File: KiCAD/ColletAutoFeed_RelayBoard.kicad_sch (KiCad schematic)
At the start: 2 parts, among them J1 690367191672, U2 ProS3

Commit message: Added 24v Monitor Circuit
Added hierarchical sheet with 24v monitor circuit. Added 4 pin power connector for 24v input. Same family connector as ribbon cable connector for relay to solenoid connections out to daughter board.
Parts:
- added J2: 690367190472, 690367190472:690367190472, symbol WR-MM-4-Female:690367190472
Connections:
- net GND: now also J2.2, J2.4
- net IO12: now reaches U2.17 (IO12)
- new net +24V: J2.1, J2.3
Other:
- added sheet 24v Monitor Circuit (24v_Monitor_Circuit.kicad_sch)
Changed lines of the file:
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@@
   (junction (at 60.96 135.89) (diameter 0) (color 0 0 0 0)
   )
+  (junction (at 100.33 135.89) (diameter 0) (color 0 0 0 0)
+  )
   (junction (at 45.72 135.89) (diameter 0) (color 0 0 0 0)
   )
   (junction (at 40.64 135.89) (diameter 0) (color 0 0 0 0)
   )
+  (junction (at 102.87 125.73) (diameter 0) (color 0 0 0 0)
+  )
   (junction (at 71.12 135.89) (diameter 0) (color 0 0 0 0)
   )
@@
     (stroke (width 0) (type default))
   )
+  (wire (pts (xy 97.79 125.73) (xy 102.87 125.73))
+    (stroke (width 0) (type default))
+  )
   (wire (pts (xy 182.88 95.25) (xy 182.88 104.14))
     (stroke (width 0) (type default))
@@
     (stroke (width 0) (type default))
   )
+  (wire (pts (xy 95.25 135.89) (xy 100.33 135.89))
+    (stroke (width 0) (type default))
+  )
   (wire (pts (xy 135.89 71.12) (xy 135.89 81.28))
     (stroke (width 0) (type default))
@@
     (stroke (width 0) (type default))
   )
+  (wire (pts (xy 85.09 27.94) (xy 96.52 27.94))
+    (stroke (width 0) (type default))
+  )
   (wire (pts (xy 45.72 135.89) (xy 50.8 135.89))
     (stroke (width 0) (type default))
@@
     (stroke (width 0) (type default))
   )
+  (wire (pts (xy 85.09 35.56) (xy 96.52 35.56))
+    (stroke (width 0) (type default))
+  )
   (wire (pts (xy 55.88 135.89) (xy 60.96 135.89))
     (stroke (width 0) (type default))
   )
+  (wire (pts (xy 25.4 45.72) (xy 25.4 57.15))
+    (stroke (width 0) (type default))
+  )
   (wire (pts (xy 179.07 71.12) (xy 179.07 81.28))
     (stroke (width 0) (type default))
@@
     (effects (font (size 1.27 1.27)) (justify left bottom))
   )
+  (label "IO12" (at 85.09 35.56 0) (fields_autoplaced)
+    (effects (font (size 1.27 1.27)) (justify left bottom))
+  )
   (label "IO0" (at 153.67 71.12 270) (fields_autoplaced)
     (effects (font (size 1.27 1.27)) (justify right bottom))
@@
     (effects (font (size 1.27 1.27)) (justify right bottom))
   )
+  (label "IO12" (at 25.4 57.15 90) (fields_autoplaced)
+    (effects (font (size 1.27 1.27)) (justify left bottom))
+  )
   (label "S4" (at 96.52 104.14 90) (fields_autoplaced)
     (effects (font (size 1.27 1.27)) (justify left bottom))
@@
   )
   (label "IO4" (at 48.26 57.15 90) (fields_autoplaced)
+    (effects (font (size 1.27 1.27)) (justify left bottom))
+  )
+  (label "MCU 3.3v" (at 85.09 27.94 0) (fields_autoplaced)
     (effects (font (size 1.27 1.27)) (justify left bottom))
   )
@@
     )
   )
+  (symbol (lib_id "power:GND") (at 100.33 135.89 0) (unit 1)
+    (in_bom yes) (on_board yes) (dnp no) (fields_autoplaced)
+    (property "Reference" "#PWR013" (at 100.33 142.24 0)
+      (effects (font (size 1.27 1.27)) hide)
+    )
+    (property "Value" "GND" (at 100.33 140.97 0)
+      (effects (font (size 1.27 1.27)))
+    )
+    (property "Footprint" "" (at 100.33 135.89 0)
+      (effects (font (size 1.27 1.27)) hide)
+    )
+    (property "Datasheet" "" (at 100.33 135.89 0)
+      (effects (font (size 1.27 1.27)) hide)
+    )
+    (pin "1")
+    (instances
+      (project "ColletAutoFeed_RelayBoard"
+        (path "/603d0a2e-fca7-40af-8fa8-51b59d823d4d"
+          (reference "#PWR013") (unit 1)
+        )
+      )
+    )
+  )
+  (symbol (lib_id "WR-MM-4-Female:690367190472") (at 100.33 130.81 0) (unit 1)
+    (in_bom yes) (on_board yes) (dnp no) (fields_autoplaced)
+    (property "Reference" "J2" (at 105.41 129.54 0)
+      (effects (font (size 1.27 1.27)) (justify left))
+    )
+    (property "Value" "690367190472" (at 105.41 132.08 0)
+      (effects (font (size 1.27 1.27)) (justify left))
+    )
+    (property "Footprint" "690367190472:690367190472" (at 100.33 130.81 0)
+      (effects (font (size 1.27 1.27)) (justify bottom) hide)
+    )
+    (property "Datasheet" "" (at 100.33 130.81 0)
+      (effects (font (size 1.27 1.27)) hide)
+    )
+    (property "MF" "Wurth Elektronik" (at 100.33 130.81 0)
+      (effects (font (size 1.27 1.27)) (justify bottom) hide)
+    )
+    (property "Description" "\n4 Position Receptacle Connector 0.100 (2.54mm) Through Hole Tin\n" (at 100.33 130.81 0)
+      (effects (font (size 1.27 1.27)) (justify bottom) hide)
+    )
+    (property "Package" "None" (at 100.33 130.81 0)
+      (effects (font (size 1.27 1.27)) (justify bottom) hide)
+    )
+    (property "Purchase-URL" "https://www.snapeda.com/api/url_track_click_mouser/?unipart_id=4618894&manufacturer=Wurth Elektronik&part_name=690367190472&search_term=690367190472" (at 100.33 130.81 0)
+      (effects (font (size 1.27 1.27)) (justify bottom) hide)
+    )
+    (property "GENDER" "Female" (at 100.33 130.81 0)
+      (effects (font (size 1.27 1.27)) (justify bottom) hide)
+    )
+    (property "Price" "None" (at 100.33 130.81 0)
+      (effects (font (size 1.27 1.27)) (justify bottom) hide)
+    )
+    (property "IR" "1.5A" (at 100.33 130.81 0)
+      (effects (font (size 1.27 1.27)) (justify bottom) hide)
+    )
+    (property "VALUE" "690367190472" (at 100.33 130.81 0)
+      (effects (font (size 1.27 1.27)) (justify bottom) hide)
+    )
+    (property "PACKAGING" "Tube" (at 100.33 130.81 0)
+      (effects (font (size 1.27 1.27)) (justify bottom) hide)
+    )
+    (property "PINS" "4" (at 100.33 130.81 0)
+      (effects (font (size 1.27 1.27)) (justify bottom) hide)
+    )
+    (property "SnapEDA_Link" "https://www.snapeda.com/parts/690367190472/Wurth+Elektronik/view-part/?ref=snap" (at 100.33 130.81 0)
+      (effects (font (size 1.27 1.27)) (justify bottom) hide)
+    )
+    (property "DATASHEET-URL" "https://www.we-online.com/catalog/datasheet/690367190472.pdf" (at 100.33 130.81 0)
+      (effects (font (size 1.27 1.27)) (justify bottom) hide)
+    )
+    (property "MP" "690367190472" (at 100.33 130.81 0)
+      (effects (font (size 1.27 1.27)) (justify bottom) hide)
+    )
+    (property "PITCH" "2.54" (at 100.33 130.81 0)
+      (effects (font (size 1.27 1.27)) (justify bottom) hide)
+    )
+    (property "PART-NUMBER" "690367190472" (at 100.33 130.81 0)
+      (effects (font (size 1.27 1.27)) (justify bottom) hide)
+    )
+    (property "TYPE" "Straight" (at 100.33 130.81 0)
+      (effects (font (size 1.27 1.27)) (justify bottom) hide)
+    )
+    (property "Availability" "In Stock" (at 100.33 130.81 0)
+      (effects (font (size 1.27 1.27)) (justify bottom) hide)
+    )
+    (property "Check_prices" "https://www.snapeda.com/parts/690367190472/Wurth+Elektronik/view-part/?ref=eda" (at 100.33 130.81 0)
+      (effects (font (size 1.27 1.27)) (justify bottom) hide)
+    )
+    (pin "2")
+    (pin "3")
+    (pin "1")
+    (pin "4")
+    (instances
+      (project "ColletAutoFeed_RelayBoard"
+        (path "/603d0a2e-fca7-40af-8fa8-51b59d823d4d"
+          (reference "J2") (unit 1)
+        )
+      )
+    )
+  )
   (symbol (lib_id "power:GND") (at 71.12 135.89 0) (unit 1)
     (in_bom yes) (on_board yes) (dnp no) (fields_autoplaced)
@@
         (path "/603d0a2e-fca7-40af-8fa8-51b59d823d4d"
           (reference "#PWR01") (unit 1)
+        )
+      )
+    )
+  )
+  (symbol (lib_id "power:+24V") (at 102.87 125.73 0) (unit 1)
+    (in_bom yes) (on_board yes) (dnp no) (fields_autoplaced)
+    (property "Reference" "#PWR014" (at 102.87 129.54 0)
+      (effects (font (size 1.27 1.27)) hide)
+    )
+    (property "Value" "+24V" (at 102.87 120.65 0)
+      (effects (font (size 1.27 1.27)))
+    )
+    (property "Footprint" "" (at 102.87 125.73 0)
+      (effects (font (size 1.27 1.27)) hide)
+    )
+    (property "Datasheet" "" (at 102.87 125.73 0)
+      (effects (font (size 1.27 1.27)) hide)
+    )
+    (pin "1")
+    (instances
+      (project "ColletAutoFeed_RelayBoard"
+        (path "/603d0a2e-fca7-40af-8fa8-51b59d823d4d"
+          (reference "#PWR014") (unit 1)
         )
       )
@@
       )
     )
+  )
+  (sheet (at 96.52 25.4) (size 12.7 13.97) (fields_autoplaced)
+    (stroke (width 0.1524) (type solid))
+    (fill (color 0 0 0 0.0000))
+    (property "Sheetname" "24v Monitor Circuit" (at 96.52 24.6884 0)
+      (effects (font (size 1.27 1.27)) (justify left bottom))
+    )
+    (property "Sheetfile" "24v_Monitor_Circuit.kicad_sch" (at 96.52 39.9546 0)
+      (effects (font (size 1.27 1.27)) (justify left top))
+    )
+    (pin "MCU 3.3v" input (at 96.52 27.94 180)
+      (effects (font (size 1.27 1.27)) (justify left))
+    )
+    (pin "MCU GPIO" output (at 96.52 35.56 180)
+      (effects (font (size 1.27 1.27)) (justify left))
+    )
+    (instances
+      (project "ColletAutoFeed_RelayBoard"
+        (path "/603d0a2e-fca7-40af-8fa8-51b59d823d4d" (page "10"))
+      )
+    )

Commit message: Ran Annotation and ERC
Annotated and ran Electronics Rules Checker. Started assigning footprints and appropriate step files to said footprints. Added custom KiCAD library folder to Github.
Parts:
- removed J1: 690367191672, 690367191672:690367191672, symbol WR-MM-16-Female:690367191672
- removed J2: 690367190472, 690367190472:690367190472, symbol WR-MM-4-Female:690367190472
- removed U2: ProS3, symbol ProS3:ProS3
- added J1: 690367191672, WR-MM:690367191672, symbol WR-MM-16:690367191672
- added J2: 690367190472, WR-MM:690367190472, symbol WR-MM-04:690367190472
- added U1: ProS3, ProS3:ProS3_TH, symbol ProS3:ProS3
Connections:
- net +24V: now also J2.1, J2.3
- net GND: now also J1.10, J1.12, J1.14, J1.16, J1.2, J1.4, J1.6, J1.8, J2.2, J2.4
- net IO0: now also U1.11 (IO0)
- net IO1: now also U1.5 (IO1)
- net IO12: now also U1.17 (IO12)
- net IO16: now also U1.13 (IO16)
- net IO2: now also U1.6 (IO2)
- net IO21: now also U1.10 (IO21)
- net IO3: now also U1.7 (IO3)
- net IO4: now also U1.8 (IO4)
- net IO5: now also U1.9 (IO5)
- net MCU 3.3v: now also U1.4 (3V3)
- net S1: now also J1.1
- net S2: now also J1.3
- net S3: now also J1.5
- net S4: now also J1.7
- net S5: now also J1.9
- net S6: now also J1.11
- net S7: now also J1.13
- net S8: now also J1.15
- no-connect marks 0 -> 24

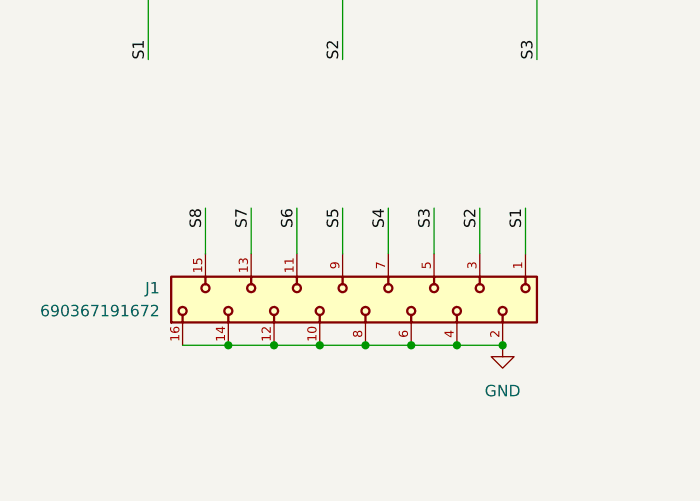
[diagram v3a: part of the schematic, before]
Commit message: Switched to TE AMP-Latch connector
Removed Wurth ribbon cable connector and replaced with TE AMP-Latch connector after physically evaluating both.
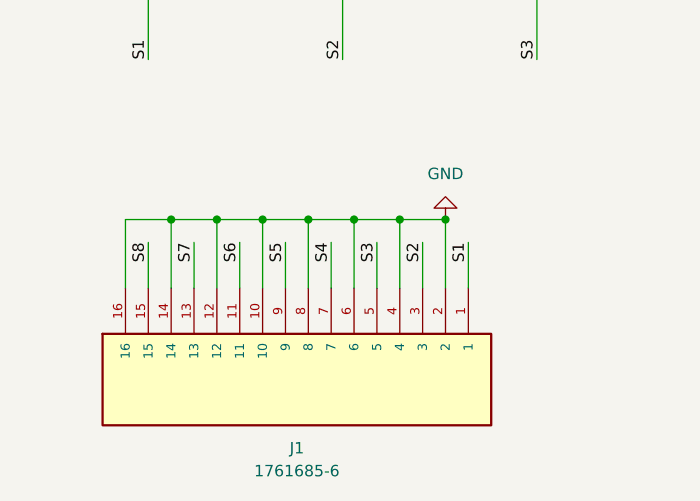
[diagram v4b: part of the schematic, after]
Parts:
- removed J1: 690367191672, WR-MM:690367191672, symbol WR-MM-16:690367191672
- added J1: 1761685-6, 1761685-6:TE_1761685-6, symbol Vertical Header - Locking:1761685-6
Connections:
- net GND: now also J1.10, J1.12, J1.14, J1.16, J1.2, J1.4, J1.6, J1.8
- net S1: now also J1.1
- net S2: now also J1.3
- net S3: now also J1.5
- net S4: now also J1.7
- net S5: now also J1.9
- net S6: now also J1.11
- net S7: now also J1.13
- net S8: now also J1.15

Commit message: Assigned footprint to pin header
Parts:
- J1: footprint 1761685-6:TE_1761685-6 -> Vertical Header - Locking:TE_1761685-6
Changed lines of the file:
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@@
       (effects (font (size 1.27 1.27)))
     )
-    (property "Footprint" "1761685-6:TE_1761685-6" (at 46.99 139.7 0)
+    (property "Footprint" "Vertical Header - Locking:TE_1761685-6" (at 46.99 139.7 0)
       (effects (font (size 1.27 1.27)) (justify bottom) hide)
     )

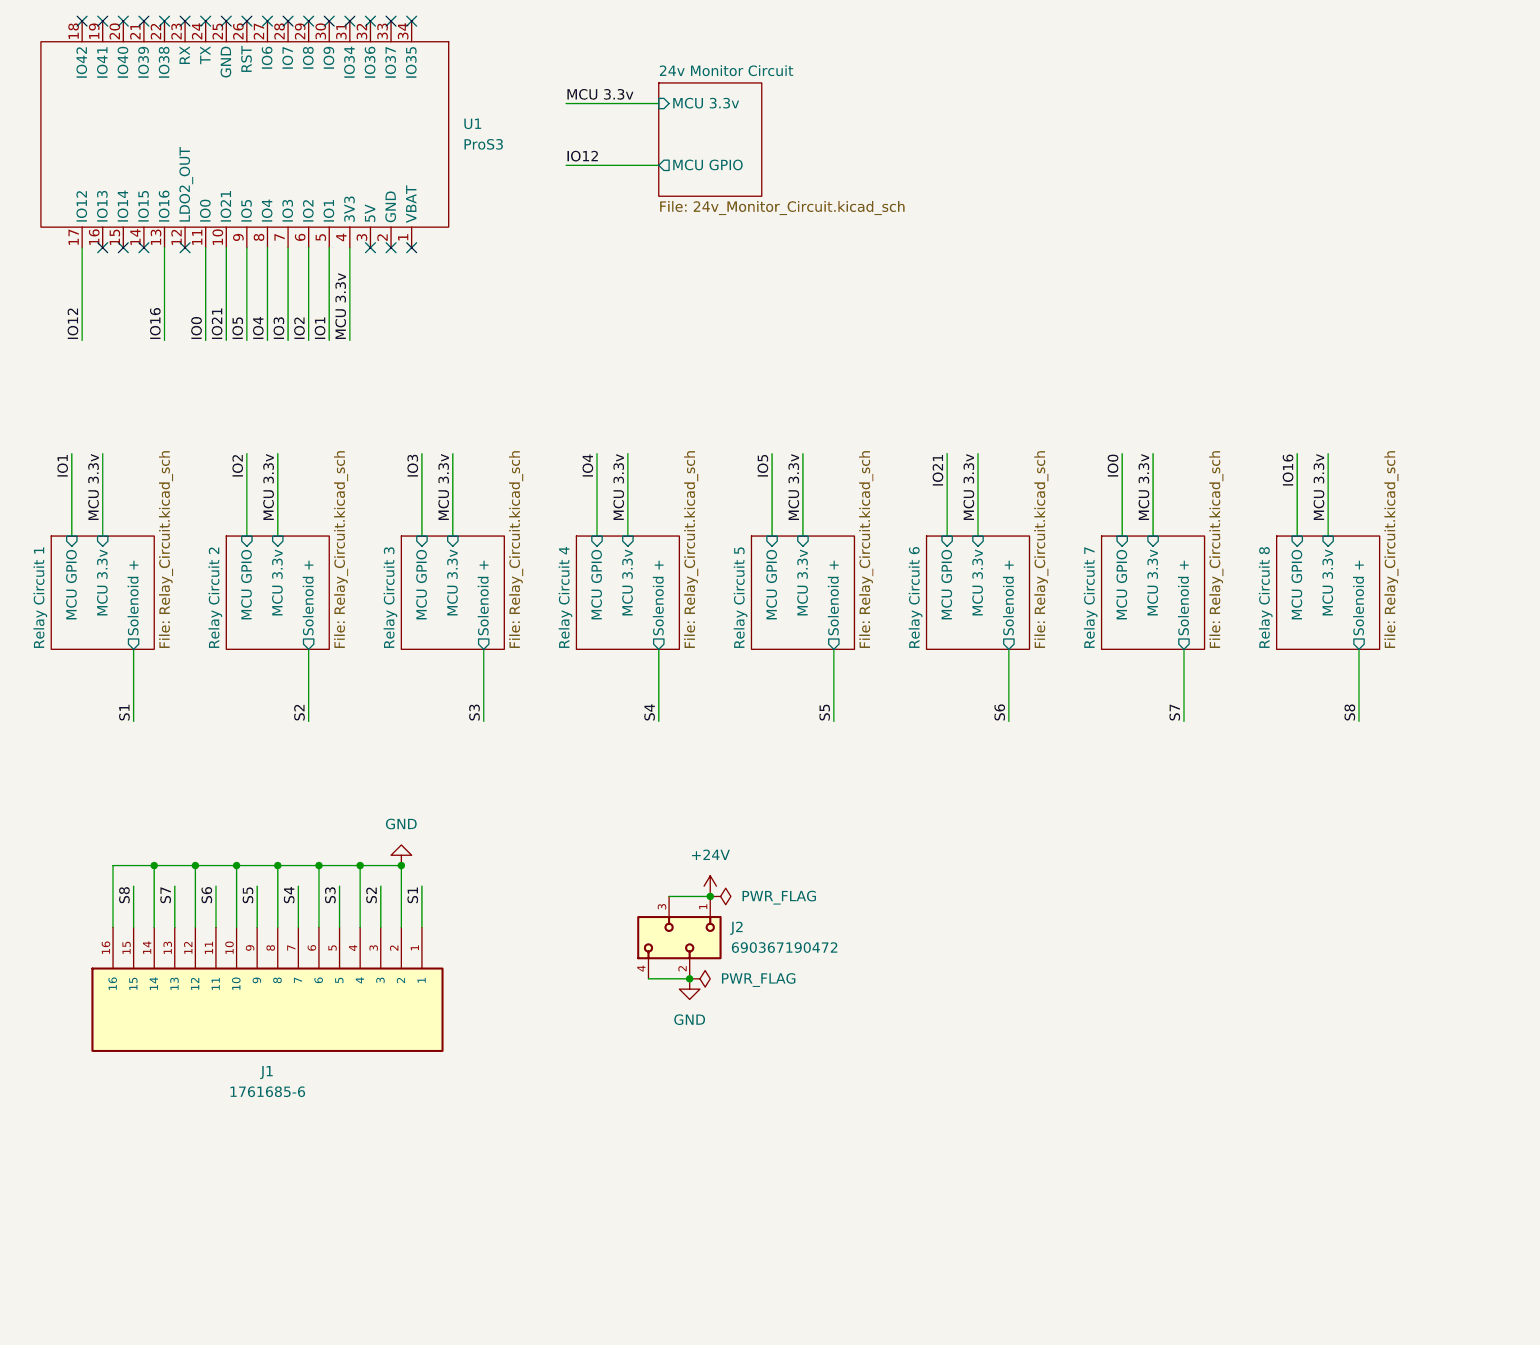
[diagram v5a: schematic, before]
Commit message: Added borders and labels to schematic
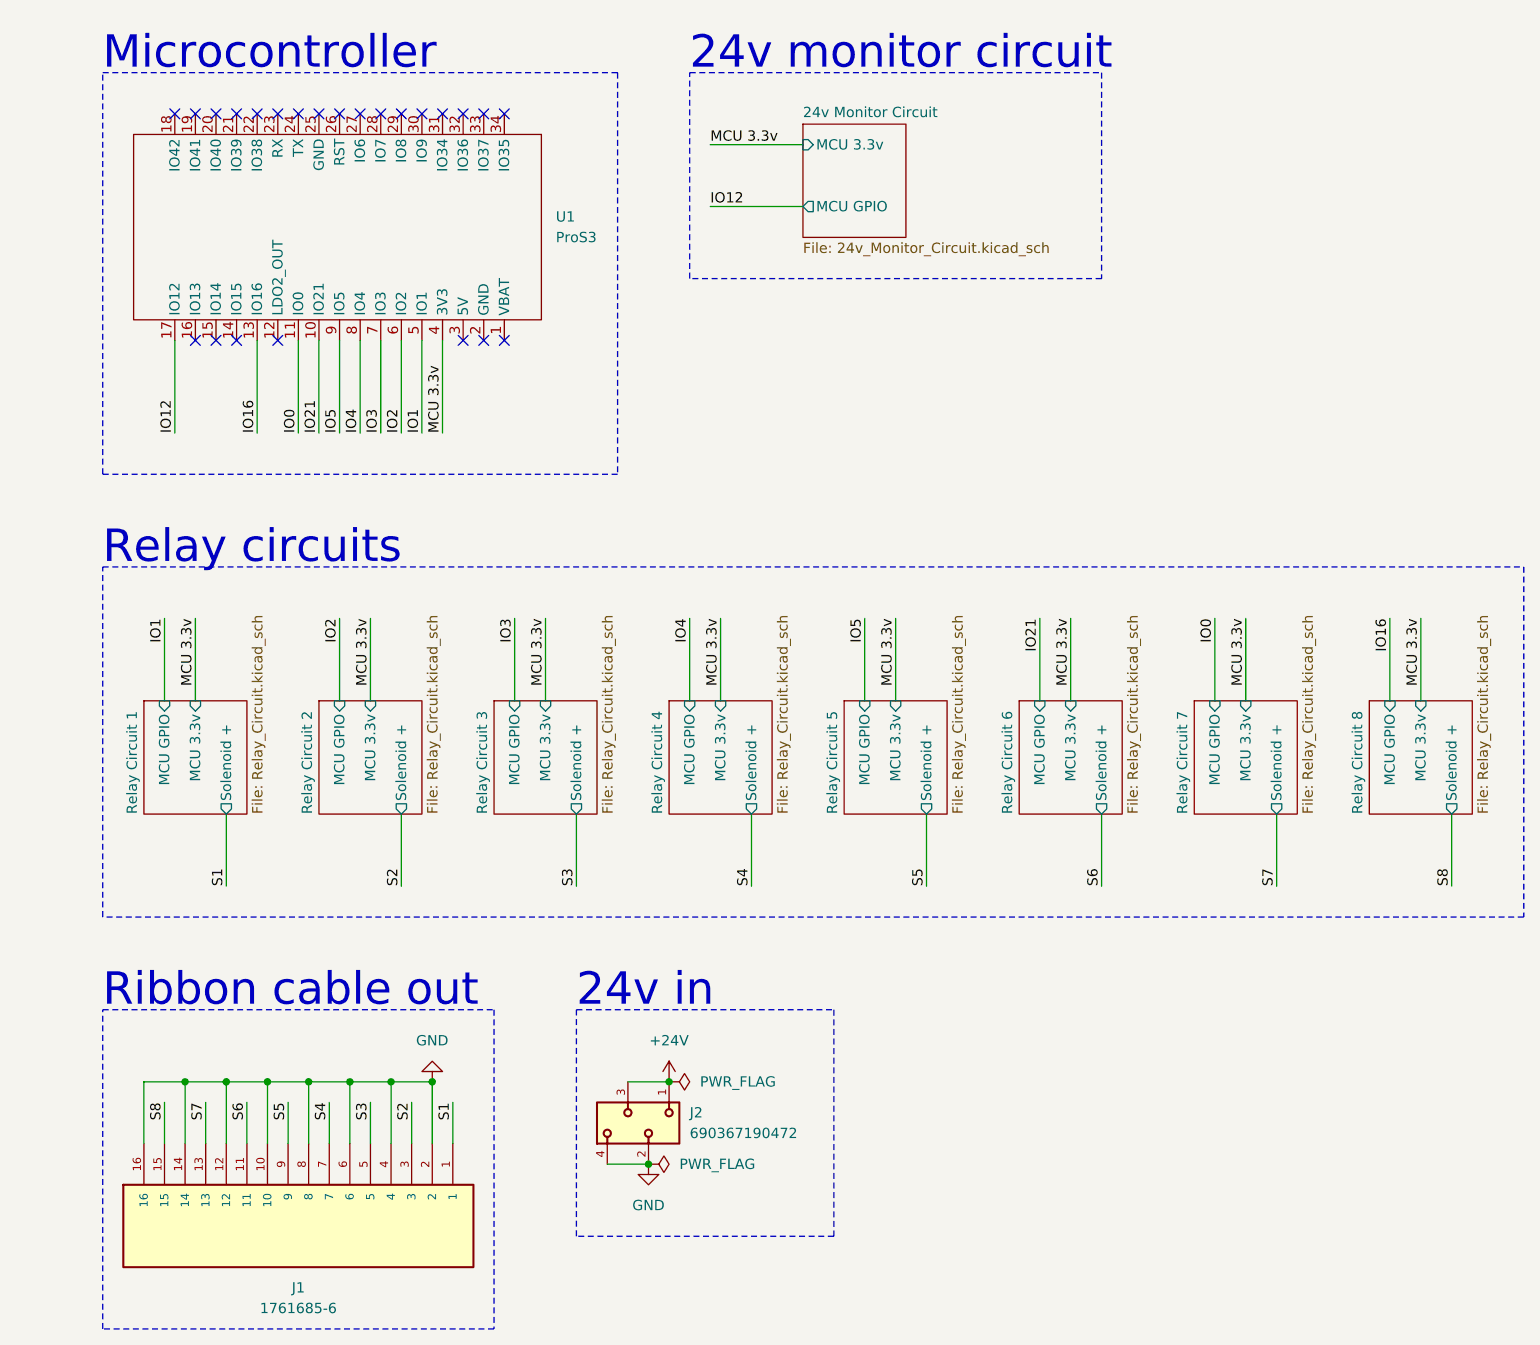
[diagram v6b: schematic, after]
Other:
- note added: "24v in"
- note added: "24v monitor circuit"
- note added: "Microcontroller"
- note added: "Relay circuits"
- note added: "Ribbon cable out"
- moved on the sheet: J1, J2, U1

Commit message: Started PCB layout
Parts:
- removed J2: 690367190472, WR-MM:690367190472, symbol WR-MM-04:690367190472
- added J2: 2068320202, Molex 206832-0202:MOLEX_2068320202, symbol Molex 206832-0202:2068320202
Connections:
- net +24V: now also J2.1
- net GND: now also J2.2
